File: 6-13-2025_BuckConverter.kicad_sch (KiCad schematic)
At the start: 17 parts, among them J1 6V to 35V, J2 5V 3A, U1 MP2338GTL-Z

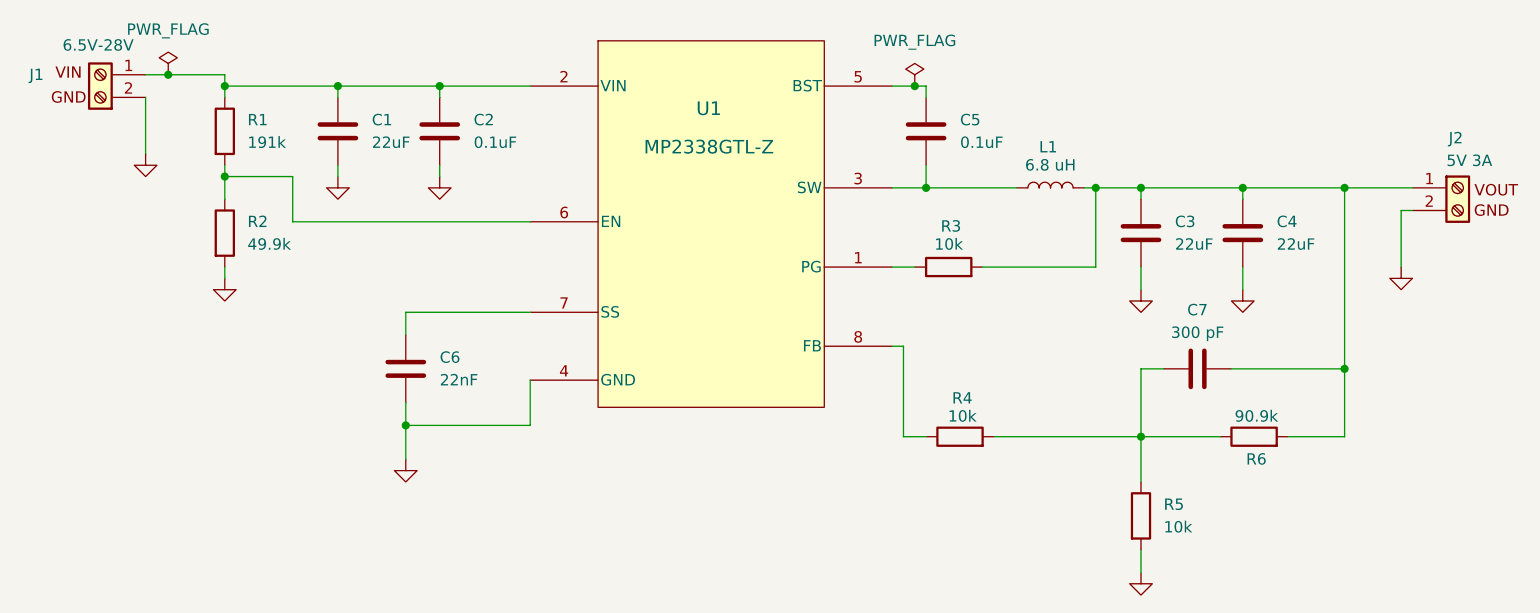
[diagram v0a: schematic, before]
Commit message: Updated PCB layout, generated prototype gerber and drill files.
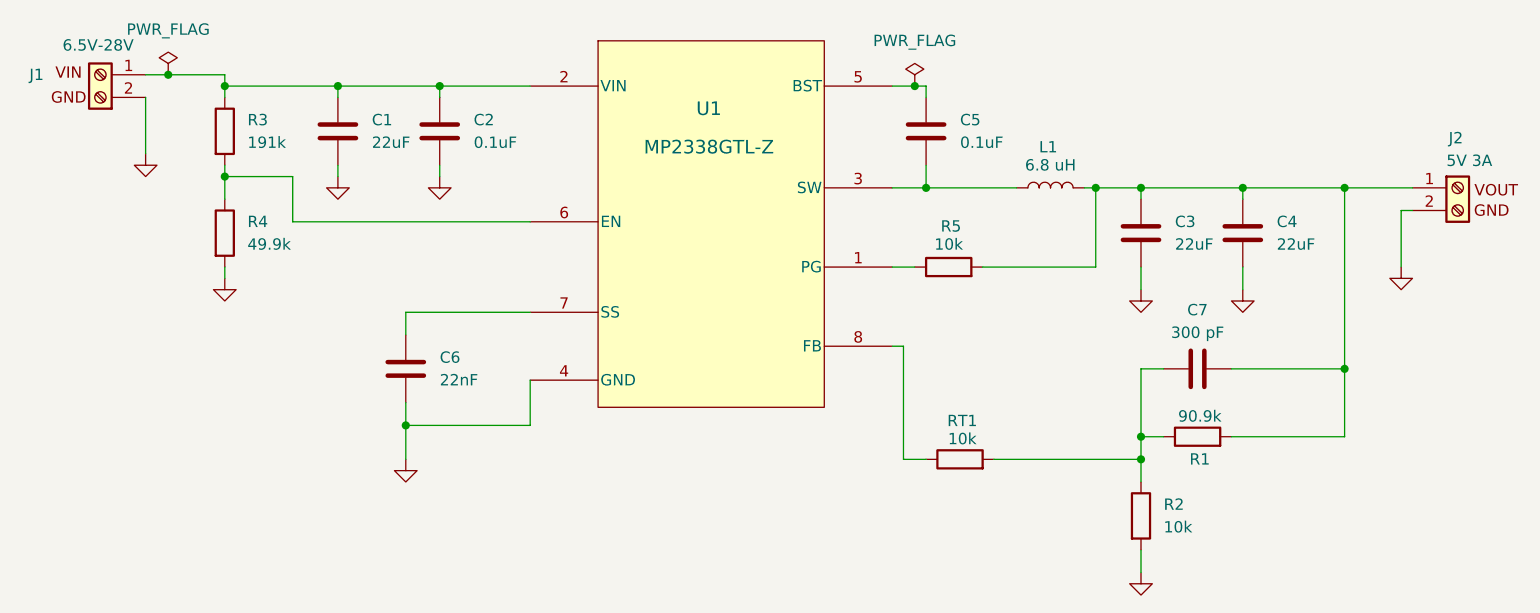
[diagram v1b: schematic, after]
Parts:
- J1, J2: footprint AlphaF:screw terminal -> AlphaF:TERM BLK 2POS SIDE ENTRY
- L1: footprint AlphaF:inductor -> AlphaF:FIXED IND 6.8UH 4.5A
- renumbered R6 to R1, R5 to R2, R1 to R3, R2 to R4, R3 to R5, R4 to RT1
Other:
- moved on the sheet: R1, RT1
